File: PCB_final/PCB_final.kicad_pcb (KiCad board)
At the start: 4 copper layers, 90 x 95 mm, 116 parts, among them J1 02x30_Shift_Register_Connector, J2 02x30_ADC_Connector, J5 PicoPinSocketB, J6 PicoPinSocketA, U1 74HC595, U10 LM321, U2 74HC595, U3 74HC595, U4 74HC595, U5 74HC595, U6 74HC595, U7 74HC595, U8 MAX11643EEG, U9 MAX11643EEG

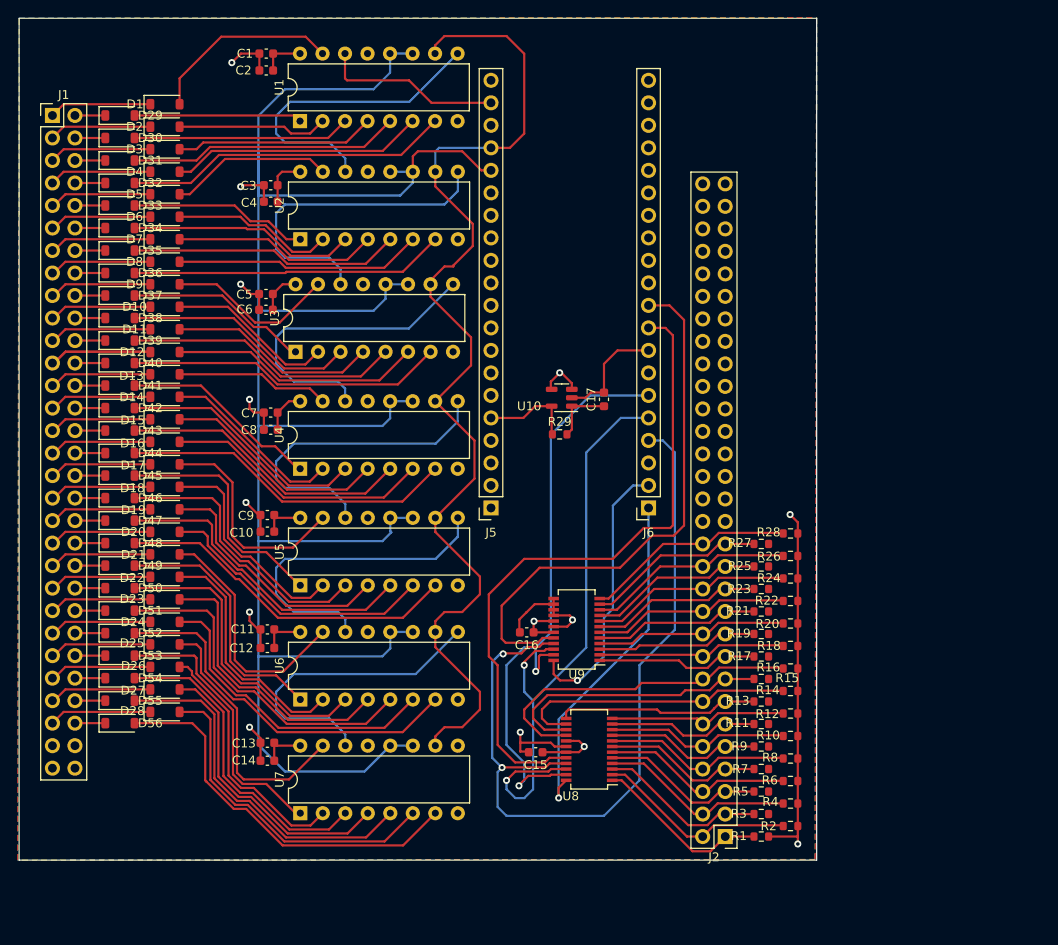
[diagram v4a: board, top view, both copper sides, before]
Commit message: Fixed all silkscreen warnings on PCB. Validated PCB. Added mounting holes to PCB.
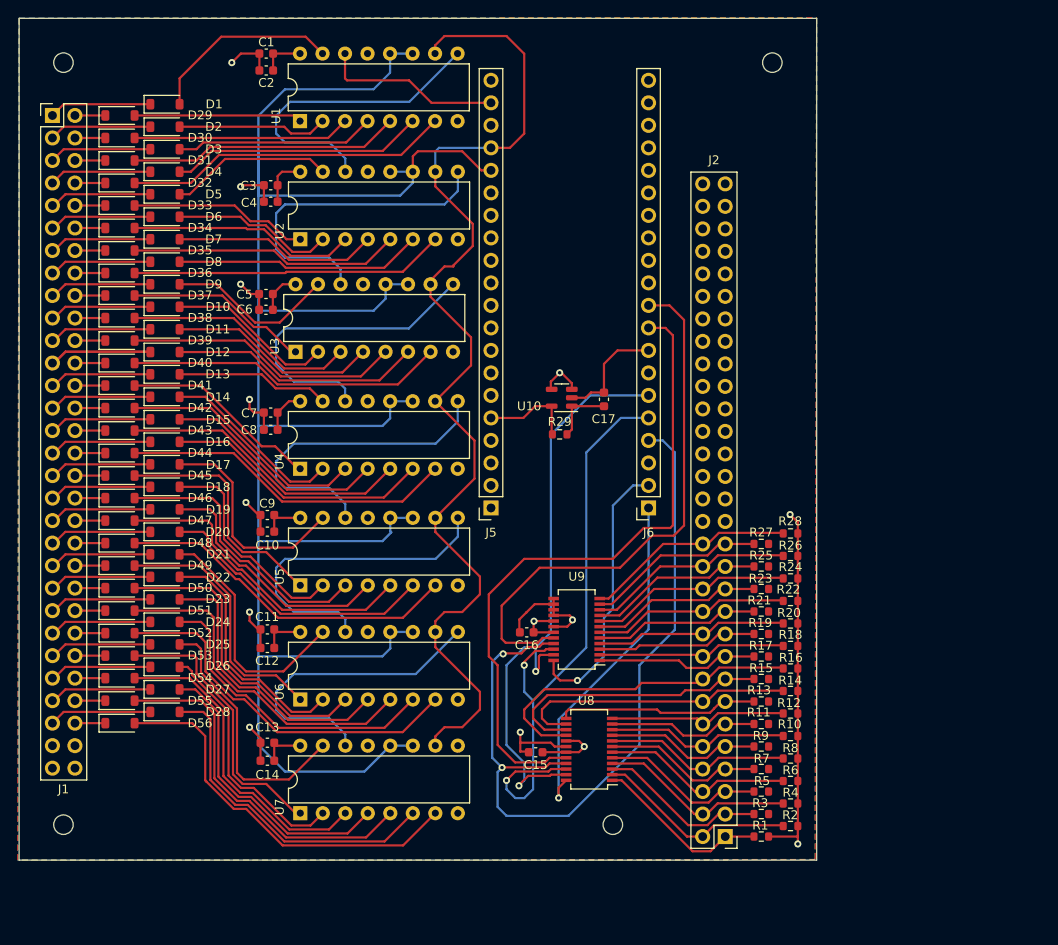
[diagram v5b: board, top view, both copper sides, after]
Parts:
- added REF**: MountingHole_2.2mm_M2, MountingHole:MountingHole_2.2mm_M2, F.Cu at (160.0, 151.0)
- added REF**: MountingHole_2.2mm_M2, MountingHole:MountingHole_2.2mm_M2, F.Cu at (178.0, 65.0)
- added REF**: MountingHole_2.2mm_M2, MountingHole:MountingHole_2.2mm_M2, F.Cu at (98.0, 151.0)
- added REF**: MountingHole_2.2mm_M2, MountingHole:MountingHole_2.2mm_M2, F.Cu at (98.0, 65.0)
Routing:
- net /Interface Board/SPI0_SCK: track 92.7 -> 90.4 mm

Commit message: Added MCP6001 PCB
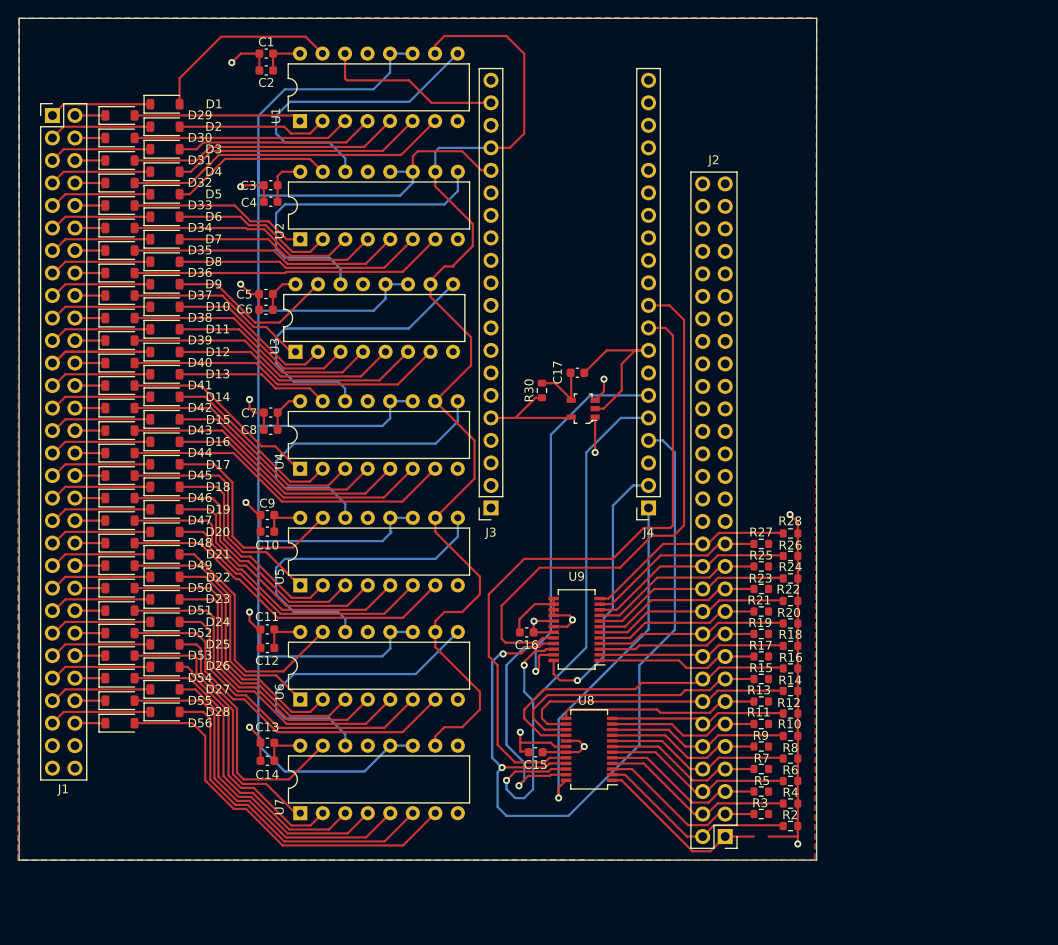
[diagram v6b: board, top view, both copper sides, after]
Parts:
- removed R1, R29: 100k, Resistor_SMD:R_0603_1608Metric
- removed REF** (x4): MountingHole_2.2mm_M2, MountingHole:MountingHole_2.2mm_M2
- added R30: 100k, Resistor_SMD:R_0603_1608Metric, F.Cu at (152.0, 102.0)
- U10: value LM321 -> MCP6001T-I_OT; footprint Package_TO_SOT_SMD:SOT-23-5 -> digikey-footprints:SOT-753
- moved C17 4.24 mm to (156.0, 100.0), turned to 0 degrees
- moved U10 2.71 mm to (156.7, 104.0), turned to 90 degrees
- renumbered J5 to J3, J6 to J4
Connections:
- C17 pad 1: Net-(U10-+) -> Net-(C17-Pad1)
- R10 pad 1: /Interface Board/ADC_IN10 -> /Interface Board/ADC_IN9
- R11 pad 1: /Interface Board/ADC_IN11 -> /Interface Board/ADC_IN10
- R12 pad 1: /Interface Board/ADC_IN12 -> /Interface Board/ADC_IN11
- R13 pad 1: /Interface Board/ADC_IN13 -> /Interface Board/ADC_IN12
- R14 pad 1: /Interface Board/ADC_IN14 -> /Interface Board/ADC_IN13
- R15 pad 1: /Interface Board/ADC_IN15 -> /Interface Board/ADC_IN14
- R16 pad 1: /Interface Board/ADC_IN16 -> /Interface Board/ADC_IN15
- R17 pad 1: /Interface Board/ADC_IN17 -> /Interface Board/ADC_IN16
- R18 pad 1: /Interface Board/ADC_IN18 -> /Interface Board/ADC_IN17
- R19 pad 1: /Interface Board/ADC_IN19 -> /Interface Board/ADC_IN18
- R2 pad 1: /Interface Board/ADC_IN2 -> /Interface Board/ADC_IN1
- R20 pad 1: /Interface Board/ADC_IN20 -> /Interface Board/ADC_IN19
- R21 pad 1: /Interface Board/ADC_IN21 -> /Interface Board/ADC_IN20
- R22 pad 1: /Interface Board/ADC_IN22 -> /Interface Board/ADC_IN21
- R23 pad 1: /Interface Board/ADC_IN23 -> /Interface Board/ADC_IN22
- R24 pad 1: /Interface Board/ADC_IN24 -> /Interface Board/ADC_IN23
- R25 pad 1: /Interface Board/ADC_IN25 -> /Interface Board/ADC_IN24
- R26 pad 1: /Interface Board/ADC_IN26 -> /Interface Board/ADC_IN25
- R27 pad 1: /Interface Board/ADC_IN27 -> /Interface Board/ADC_IN26
- R28 pad 1: /Interface Board/ADC_IN28 -> /Interface Board/ADC_IN27
- R3 pad 1: /Interface Board/ADC_IN3 -> /Interface Board/ADC_IN2
- R4 pad 1: /Interface Board/ADC_IN4 -> /Interface Board/ADC_IN3
- R5 pad 1: /Interface Board/ADC_IN5 -> /Interface Board/ADC_IN4
- R6 pad 1: /Interface Board/ADC_IN6 -> /Interface Board/ADC_IN5
- R7 pad 1: /Interface Board/ADC_IN7 -> /Interface Board/ADC_IN6
- R8 pad 1: /Interface Board/ADC_IN8 -> /Interface Board/ADC_IN7
- R9 pad 1: /Interface Board/ADC_IN9 -> /Interface Board/ADC_IN8
- U10 pad 1: Net-(U10-+) -> +3V3
- U10 pad 4: +3V3 -> Net-(C17-Pad1)
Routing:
- net Net-(C17-Pad1): track 0.00 -> 7.19 mm
- net Net-(U10-+): track 7.04 -> 0.00 mm
- net GND: track 107.5 -> 113.5 mm
- net /Interface Board/3V3_Pico: track 10.6 -> 13.0 mm
- net +3V3: track 53.1 -> 55.0 mm, vias 3 -> 4
